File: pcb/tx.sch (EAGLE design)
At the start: 53 parts, among them U3 MCP73831T-2ACI/OT, Y1 CRYSTAL-26MHZSMD-3.2X2.5

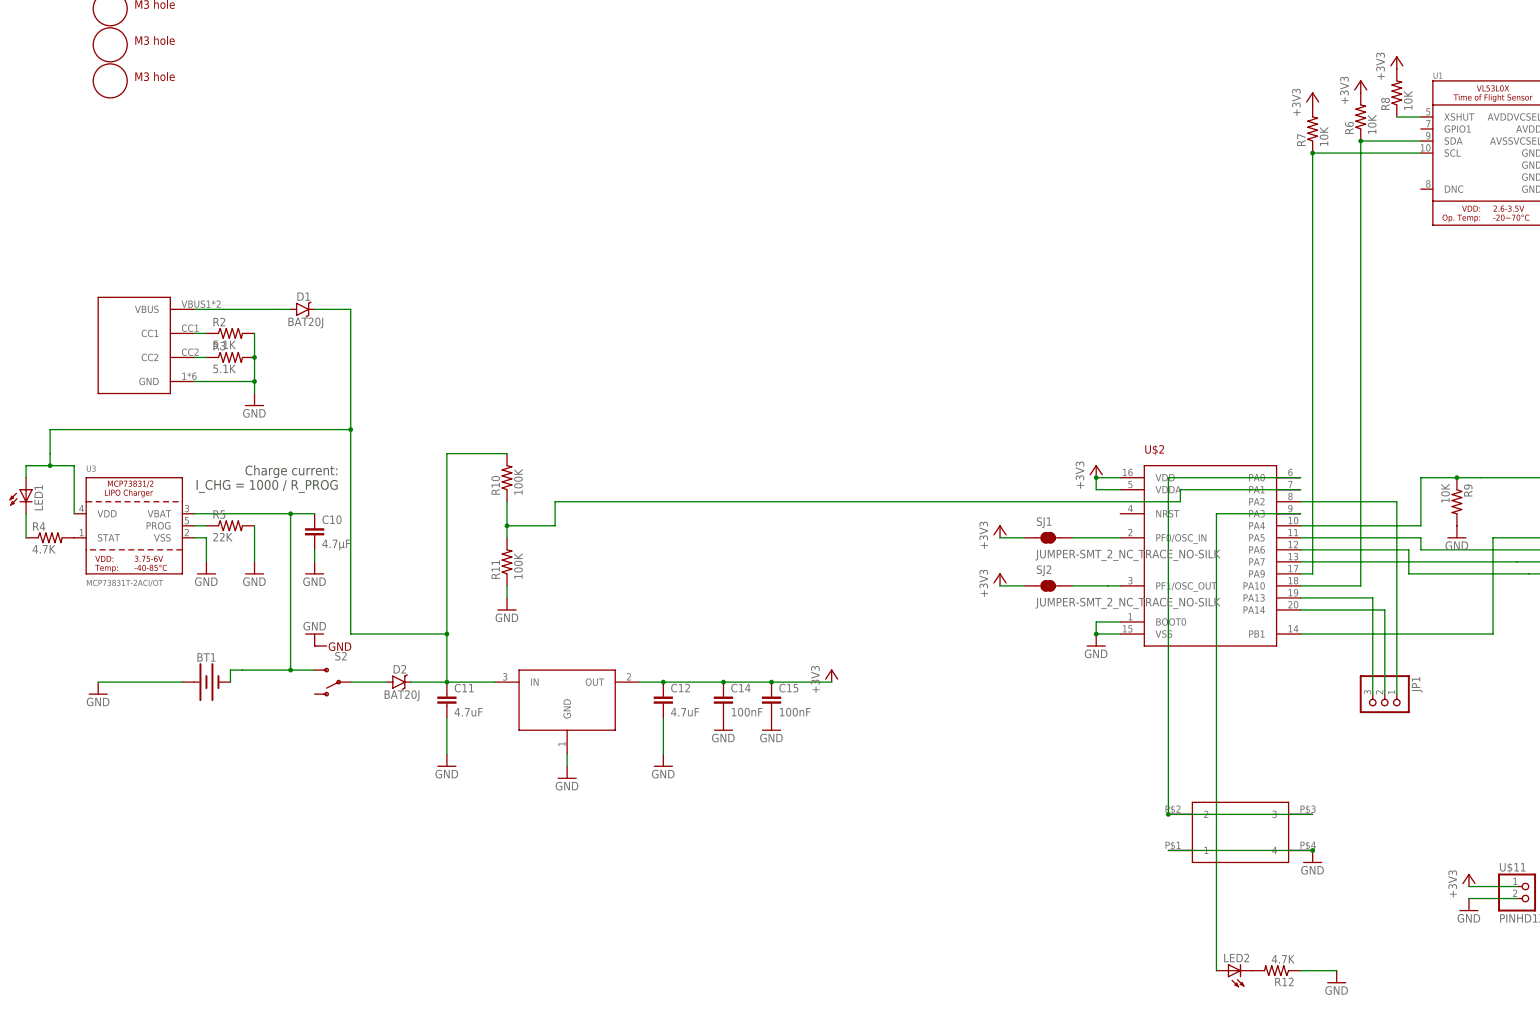
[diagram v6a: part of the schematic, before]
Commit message: thinking about switch to tssop20
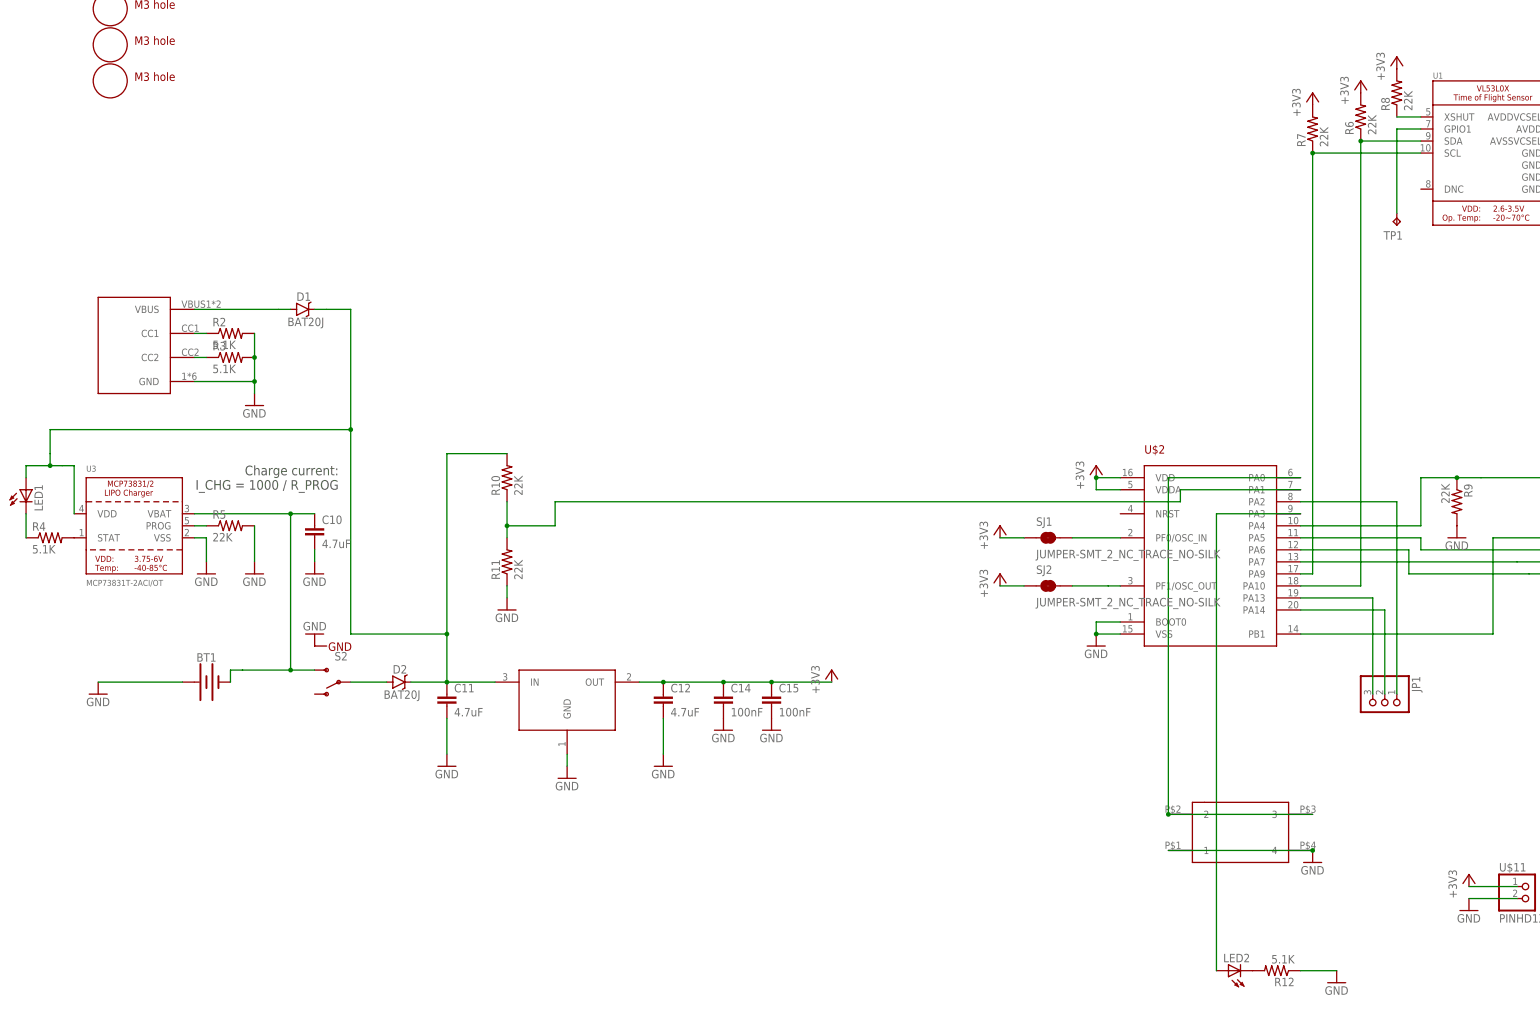
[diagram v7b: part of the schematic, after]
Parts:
- added TP1: TPTP12R, testpad:TPTP12R
- C10: value 4.7µF -> 4.7uF
- R10, R11: value 100K -> 22K
- R12, R4: value 4.7K -> 5.1K
- R6, R7, R8, R9: value 10K -> 22K
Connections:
- new net N$36: TP1.TP, U1.GPIO1
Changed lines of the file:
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@@
 <part name="R2" library="joyAnalog" deviceset="RESISTOR" device="0805-RES" value="5.1K"/>
 <part name="U3" library="microbuilder" deviceset="MCP73831/2" device="" value="MCP73831T-2ACI/OT"/>
-<part name="R4" library="SparkFun-Passives" deviceset="RESISTOR" device="0805-RES" value="4.7K"/>
-<part name="C10" library="SparkFun-Passives" deviceset="CAP" device="0805" value="4.7µF"/>
+<part name="R4" library="SparkFun-Passives" deviceset="RESISTOR" device="0805-RES" value="5.1K"/>
+<part name="C10" library="SparkFun-Passives" deviceset="CAP" device="0805" value="4.7uF"/>
 <part name="R5" library="SparkFun-Passives" deviceset="RESISTOR" device="0805-RES" value="22K"/>
 <part name="GND7" library="supply1" library_urn="urn:adsk.eagle:library:371" deviceset="GND" device=""/>
@@
 <part name="LED1" library="joyAnalog" deviceset="LED" device="CHIP-LED0805"/>
 <part name="GND18" library="clock" deviceset="GND" device=""/>
-<part name="R6" library="SparkFun-Passives" deviceset="RESISTOR" device="0805-RES" value="10K"/>
-<part name="R7" library="SparkFun-Passives" deviceset="RESISTOR" device="0805-RES" value="10K"/>
+<part name="R6" library="SparkFun-Passives" deviceset="RESISTOR" device="0805-RES" value="22K"/>
+<part name="R7" library="SparkFun-Passives" deviceset="RESISTOR" device="0805-RES" value="22K"/>
 <part name="+3V3" library="supply1" library_urn="urn:adsk.eagle:library:371" deviceset="+3V3" device=""/>
 <part name="+3V4" library="supply1" library_urn="urn:adsk.eagle:library:371" deviceset="+3V3" device=""/>
-<part name="R8" library="SparkFun-Passives" deviceset="RESISTOR" device="0805-RES" value="10K"/>
+<part name="R8" library="SparkFun-Passives" deviceset="RESISTOR" device="0805-RES" value="22K"/>
 <part name="+3V6" library="supply1" library_urn="urn:adsk.eagle:library:371" deviceset="+3V3" device=""/>
 <part name="GND19" library="clock" deviceset="GND" device=""/>
@@
 <part name="GND24" library="supply1" library_urn="urn:adsk.eagle:library:371" deviceset="GND" device=""/>
 <part name="U$10" library="3pos_slide_switch" deviceset="324_SW" device=""/>
-<part name="R9" library="joyAnalog" deviceset="RESISTOR" device="0805-RES" value="10K"/>
+<part name="R9" library="joyAnalog" deviceset="RESISTOR" device="0805-RES" value="22K"/>
 <part name="GND25" library="supply1" library_urn="urn:adsk.eagle:library:371" deviceset="GND" device=""/>
 <part name="LED2" library="joyAnalog" deviceset="LED" device="CHIP-LED0805"/>
-<part name="R12" library="joyAnalog" deviceset="RESISTOR" device="0805-RES" value="4.7K"/>
+<part name="R12" library="joyAnalog" deviceset="RESISTOR" device="0805-RES" value="5.1K"/>
 <part name="GND27" library="supply1" library_urn="urn:adsk.eagle:library:371" deviceset="GND" device=""/>
 <part name="GND28" library="supply1" library_urn="urn:adsk.eagle:library:371" deviceset="GND" device=""/>
@@
 <part name="GND29" library="clock" deviceset="GND" device=""/>
 <part name="+3V5" library="supply1" library_urn="urn:adsk.eagle:library:371" deviceset="+3V3" device=""/>
-<part name="R10" library="SparkFun-Passives" deviceset="RESISTOR" device="0805-RES" value="100K"/>
-<part name="R11" library="SparkFun-Passives" deviceset="RESISTOR" device="0805-RES" value="100K"/>
+<part name="R10" library="SparkFun-Passives" deviceset="RESISTOR" device="0805-RES" value="22K"/>
+<part name="R11" library="SparkFun-Passives" deviceset="RESISTOR" device="0805-RES" value="22K"/>
 <part name="GND30" library="supply1" library_urn="urn:adsk.eagle:library:371" deviceset="GND" device=""/>
 <part name="JP1" library="adafruit_changed" deviceset="PINHD-1X3" device="CB"/>
@@
 <part name="+3V9" library="supply1" library_urn="urn:adsk.eagle:library:371" deviceset="+3V3" device=""/>
 <part name="+3V10" library="supply1" library_urn="urn:adsk.eagle:library:371" deviceset="+3V3" device=""/>
+<part name="TP1" library="testpad" library_urn="urn:adsk.eagle:library:385" deviceset="TP" device="TP12R" package3d_urn="urn:adsk.eagle:package:27963/1" value="TPTP12R"/>
 </parts>
 <sheets>
@@
 <instance part="+3V9" gate="G$1" x="-58.42" y="-53.34"/>
 <instance part="+3V10" gate="G$1" x="-58.42" y="-63.5"/>
+<instance part="TP1" gate="G$1" x="25.4" y="10.16" rot="R180"/>
 </instances>
 <busses>
@@
 </segment>
 </net>
+<net name="N$36" class="0">
+<segment>
+<pinref part="U1" gate="G$1" pin="GPIO1"/>
+<wire x1="30.48" y1="30.48" x2="25.4" y2="30.48" width="0.1524" layer="91"/>
+<pinref part="TP1" gate="G$1" pin="TP"/>
+<wire x1="25.4" y1="30.48" x2="25.4" y2="12.7" width="0.1524" layer="91"/>
+</segment>
+</net>
 </nets>
 </sheet>
@@
 with this version.
 </note>
+<note version="8.3" severity="warning">
+Since Version 8.3, EAGLE supports URNs for individual library
+assets (packages, symbols, and devices). The URNs of those assets
+will not be understood (or retained) with this version.
+</note>
+<note version="8.3" severity="warning">
+Since Version 8.3, EAGLE supports the association of 3D packages
+with devices in libraries, schematics, and board files. Those 3D
+packages will not be understood (or retained) with this version.
+</note>
 </compatibility>

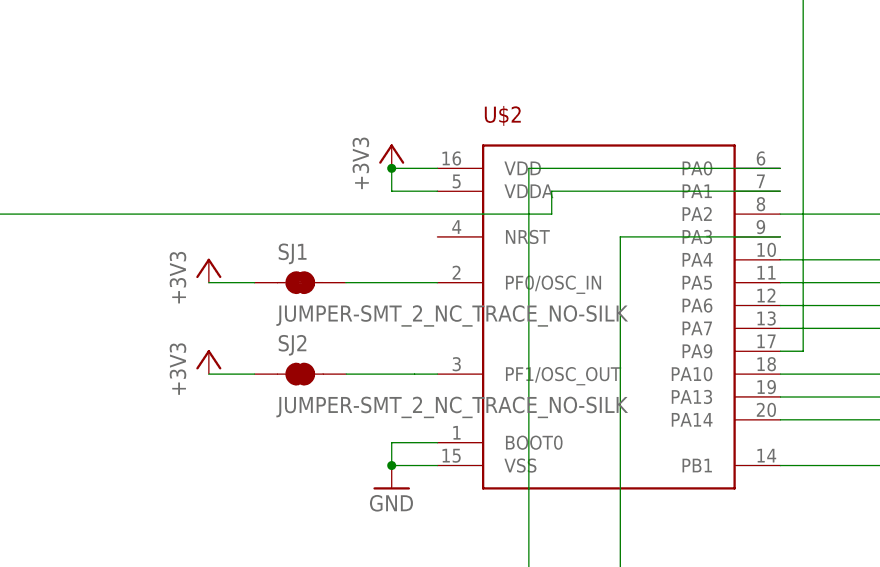
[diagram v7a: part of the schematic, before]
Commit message: switched rx to tssop20
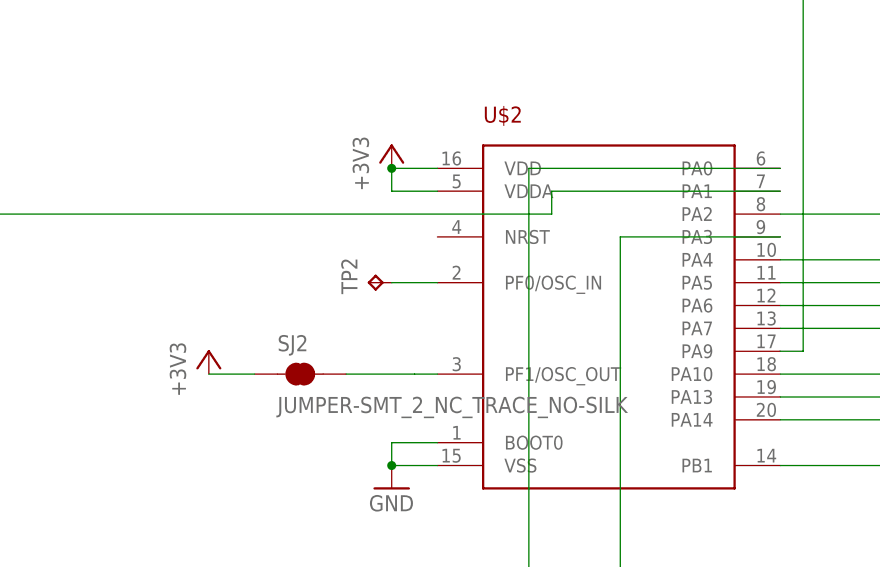
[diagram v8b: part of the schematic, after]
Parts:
- removed SJ1: JUMPER-SMT_2_NC_TRACE_NO-SILK, SparkFun-Jumpers:JUMPER-SMT_2_NC_TRACE_NO-SILK
- added TP2: TPTP12R, testpad:TPTP12R
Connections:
- removed net N$23: SJ1.2, U$2.PF0/OSC_IN
- new net N$37: TP2.TP, U$2.PF0/OSC_IN
- net +3V3: no longer SJ1.1
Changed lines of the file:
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@@
 <part name="JP1" library="adafruit_changed" deviceset="PINHD-1X3" device="CB"/>
 <part name="+3V8" library="supply1" library_urn="urn:adsk.eagle:library:371" deviceset="+3V3" device=""/>
-<part name="SJ1" library="SparkFun-Jumpers" deviceset="JUMPER-SMT_2_NC_TRACE" device="_NO-SILK"/>
 <part name="SJ2" library="SparkFun-Jumpers" deviceset="JUMPER-SMT_2_NC_TRACE" device="_NO-SILK"/>
-<part name="+3V9" library="supply1" library_urn="urn:adsk.eagle:library:371" deviceset="+3V3" device=""/>
 <part name="+3V10" library="supply1" library_urn="urn:adsk.eagle:library:371" deviceset="+3V3" device=""/>
 <part name="TP1" library="testpad" library_urn="urn:adsk.eagle:library:385" deviceset="TP" device="TP12R" package3d_urn="urn:adsk.eagle:package:27963/1" value="TPTP12R"/>
+<part name="TP2" library="testpad" library_urn="urn:adsk.eagle:library:385" deviceset="TP" device="TP12R" package3d_urn="urn:adsk.eagle:package:27963/1" value="TPTP12R"/>
 </parts>
 <sheets>
@@
 <instance part="JP1" gate="A" x="22.86" y="-91.44" rot="R270"/>
 <instance part="+3V8" gate="G$1" x="25.4" y="45.72"/>
-<instance part="SJ1" gate="G$1" x="-48.26" y="-55.88"/>
 <instance part="SJ2" gate="G$1" x="-48.26" y="-66.04"/>
-<instance part="+3V9" gate="G$1" x="-58.42" y="-53.34"/>
 <instance part="+3V10" gate="G$1" x="-58.42" y="-63.5"/>
 <instance part="TP1" gate="G$1" x="25.4" y="10.16" rot="R180"/>
+<instance part="TP2" gate="G$1" x="-40.64" y="-55.88" rot="R90"/>
 </instances>
 <busses>
@@
 <pinref part="R8" gate="G$1" pin="2"/>
 <pinref part="+3V8" gate="G$1" pin="+3V3"/>
-</segment>
-<segment>
-<pinref part="+3V9" gate="G$1" pin="+3V3"/>
-<pinref part="SJ1" gate="G$1" pin="1"/>
-<wire x1="-58.42" y1="-55.88" x2="-53.34" y2="-55.88" width="0.1524" layer="91"/>
 </segment>
 <segment>
@@
 </segment>
 </net>
-<net name="N$23" class="0">
-<segment>
-<pinref part="U$2" gate="G$1" pin="PF0/OSC_IN"/>
-<pinref part="SJ1" gate="G$1" pin="2"/>
-<wire x1="-33.02" y1="-55.88" x2="-43.18" y2="-55.88" width="0.1524" layer="91"/>
-</segment>
-</net>
 <net name="N$34" class="0">
 <segment>
@@
 </segment>
 </net>
+<net name="N$37" class="0">
+<segment>
+<pinref part="U$2" gate="G$1" pin="PF0/OSC_IN"/>
+<pinref part="TP2" gate="G$1" pin="TP"/>
+<wire x1="-33.02" y1="-55.88" x2="-38.1" y2="-55.88" width="0.1524" layer="91"/>
+</segment>
+</net>
